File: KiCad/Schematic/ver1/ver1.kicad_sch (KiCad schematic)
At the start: 1 part

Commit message: Deez nuts
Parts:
- added U1: AD797, symbol Amplifier_Operational:AD797
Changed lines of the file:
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@@
+		)
+	)
+	(symbol
+		(lib_id "Amplifier_Operational:AD797")
+		(at 165.1 71.12 0)
+		(unit 1)
+		(exclude_from_sim no)
+		(in_bom yes)
+		(on_board yes)
+		(dnp no)
+		(fields_autoplaced yes)
+		(property "Reference" "U1"
+			(at 175.26 64.8014 0)
+			(effects
+				(font
+					(size 1.27 1.27)
+				)
+			)
+		)
+		(property "Value" "AD797"
+			(at 175.26 67.3414 0)
+			(effects
+				(font
+					(size 1.27 1.27)
+				)
+			)
+		)
+		(property "Footprint" ""
+			(at 166.37 69.85 0)
+			(effects
+				(font
+					(size 1.27 1.27)
+				)
+				(hide yes)
+			)
+		)
+		(property "Datasheet" "https://www.analog.com/media/en/technical-documentation/data-sheets/AD797.pdf"
+			(at 166.37 67.31 0)
+			(effects
+				(font
+					(size 1.27 1.27)
+				)
+				(hide yes)
+			)
+		)
+		(property "Description" "Ultralow Distortion, Ultralow Noise Op Amp, DIP-8/SOIC-8"
+			(at 165.1 71.12 0)
+			(effects
+				(font
+					(size 1.27 1.27)
+				)
+				(hide yes)
+			)
+		)
+		(pin "3"
+		)
+		(pin "2"
+		)
+		(pin "5"
+		)
+		(pin "8"
+		)
+		(pin "1"
+		)
+		(pin "6"
+		)
+		(pin "4"
+		)
+		(pin "7"
+		)
+		(instances
+			(project ""
+				(path "/7dc9043a-ef1d-4623-9acc-dd1f81d56424"
+					(reference "U1")
+					(unit 1)
+				)
+			)
 		)
 	)

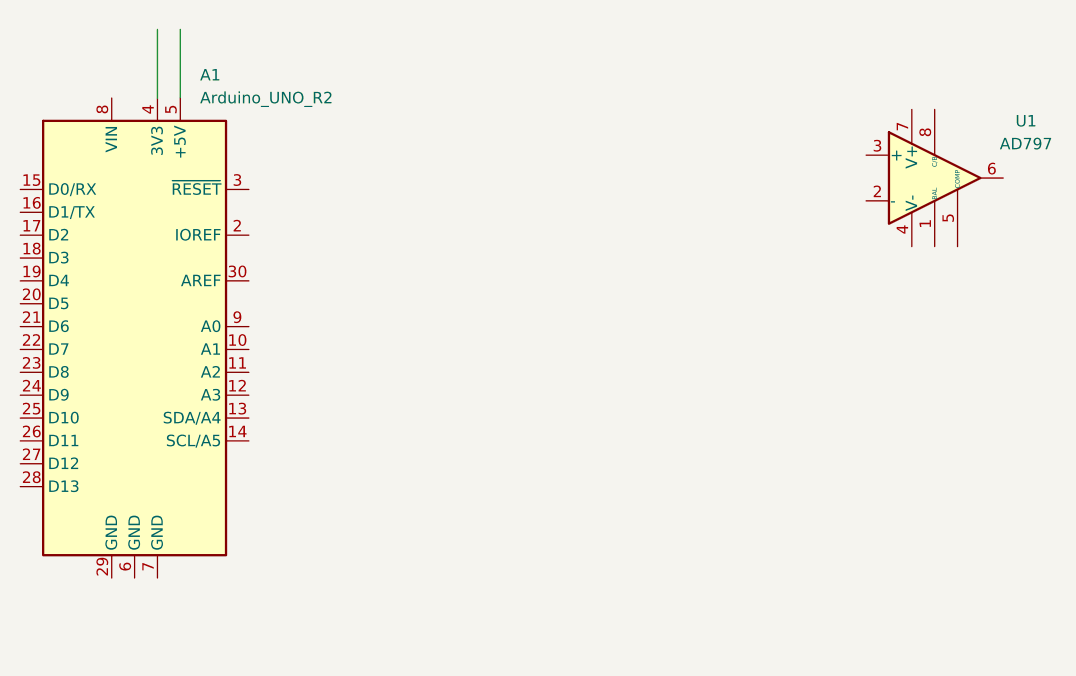
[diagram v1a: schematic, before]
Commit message: setting up arduino
battery source
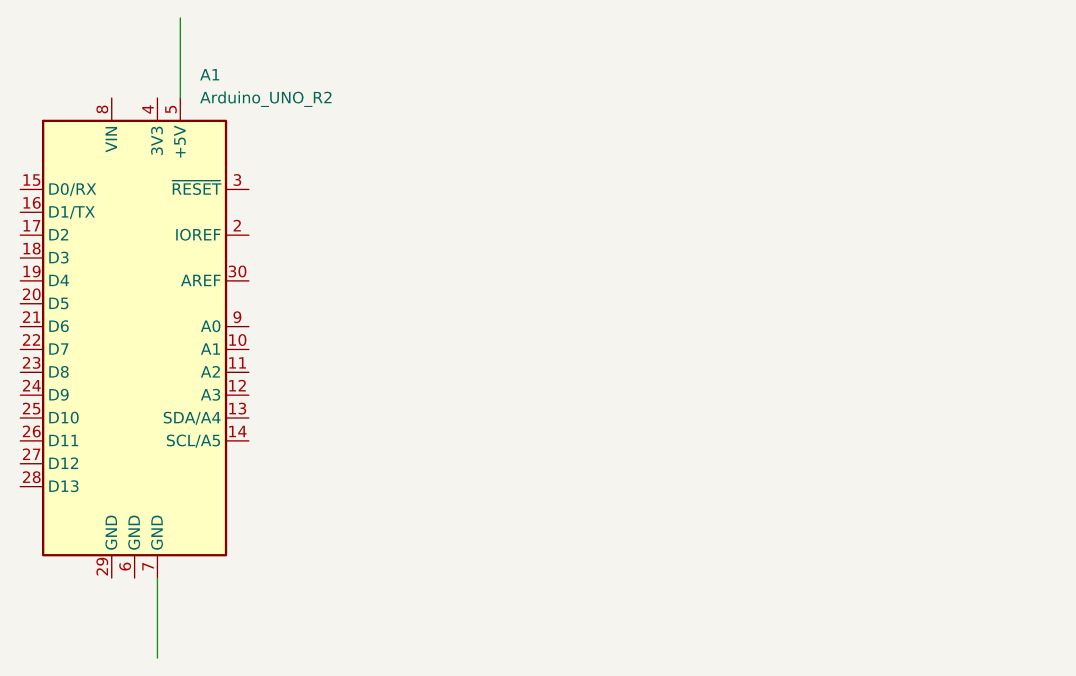
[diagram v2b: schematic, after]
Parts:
- removed U1: AD797, symbol Amplifier_Operational:AD797
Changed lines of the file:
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@@
 	(wire
 		(pts
-			(xy 78.74 54.61) (xy 78.74 62.23)
+			(xy 81.28 53.34) (xy 81.28 62.23)
 		)
 		(stroke
@@
 	(wire
 		(pts
-			(xy 81.28 54.61) (xy 81.28 62.23)
+			(xy 78.74 115.57) (xy 78.74 124.46)
 		)
 		(stroke
@@
 					(unit 1)
 				)
-			)
-		)
-	)
-	(symbol
-		(lib_id "Amplifier_Operational:AD797")
-		(at 165.1 71.12 0)
-		(unit 1)
-		(exclude_from_sim no)
-		(in_bom yes)
-		(on_board yes)
-		(dnp no)
-		(fields_autoplaced yes)
-		(property "Reference" "U1"
-			(at 175.26 64.8014 0)
-			(effects
-				(font
-					(size 1.27 1.27)
-				)
-			)
-		)
-		(property "Value" "AD797"
-			(at 175.26 67.3414 0)
-			(effects
-				(font
-					(size 1.27 1.27)
-				)
-			)
-		)
-		(property "Footprint" ""
-			(at 166.37 69.85 0)
-			(effects
-				(font
-					(size 1.27 1.27)
-				)
-				(hide yes)
-			)
-		)
-		(property "Datasheet" "https://www.analog.com/media/en/technical-documentation/data-sheets/AD797.pdf"
-			(at 166.37 67.31 0)
-			(effects
-				(font
-					(size 1.27 1.27)
-				)
-				(hide yes)
-			)
-		)
-		(property "Description" "Ultralow Distortion, Ultralow Noise Op Amp, DIP-8/SOIC-8"
-			(at 165.1 71.12 0)
-			(effects
-				(font
-					(size 1.27 1.27)
-				)
-				(hide yes)
-			)
-		)
-		(pin "3"
-		)
-		(pin "2"
-		)
-		(pin "5"
-		)
-		(pin "8"
-		)
-		(pin "1"
-		)
-		(pin "6"
-		)
-		(pin "4"
-		)
-		(pin "7"
-		)
-		(instances
-			(project ""
-				(path "/7dc9043a-ef1d-4623-9acc-dd1f81d56424"
-					(reference "U1")
-					(unit 1)
-				)

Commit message: did somethings...
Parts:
- removed A1: Arduino_UNO_R2, Module:Arduino_UNO_R2, symbol MCU_Module:Arduino_UNO_R2
- added C1: ~, symbol SparkFun Qwiic Soil Moisture Sensor-eagle-import:C-0201
- added J1: ~, SparkFun-Switch:Slide_DPDT_SMD_9.0x3.6mm, symbol SparkFun Qwiic Soil Moisture Sensor-eagle-import:JST-SH-4P-1.0
- added JP1: ~, SparkFun Qwiic Soil Moisture Sensor:2X03, symbol SparkFun Qwiic Soil Moisture Sensor-eagle-import:PINHD-2X3
- added U1: ~, SparkFun Qwiic Soil Moisture Sensor:SO08-EIAJ_MCU, symbol SparkFun Qwiic Soil Moisture Sensor-eagle-import:ATTINY85-ARDUINOTINY85-20-SMT
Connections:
- new net: J1.3 (SDA), JP1.4, U1.5 (~{(SDA/MOSI})0)
- new net: J1.4 (SCL), JP1.3, U1.7 ((SCL/SCK/A1)2)
- new net: JP1.1, U1.6 (~{(MISO})1)
- new net: JP1.5, U1.1 ((~{RESET}/A0)5)
- new net +3.3V: C1.1, J1.2 (VCC), JP1.2, U1.8 (VCC)
- new net Earth: C1.2, J1.1 (GND), J1.NC1 (5), J1.NC2 (6), JP1.6, U1.4 (GND)
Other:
- note added: "07.07.2024"
- note added: "Patrick"
- note added: "Plantifier - Ardunio Prototype"
- note added: "Samuel"
- note added: "alpha-001"

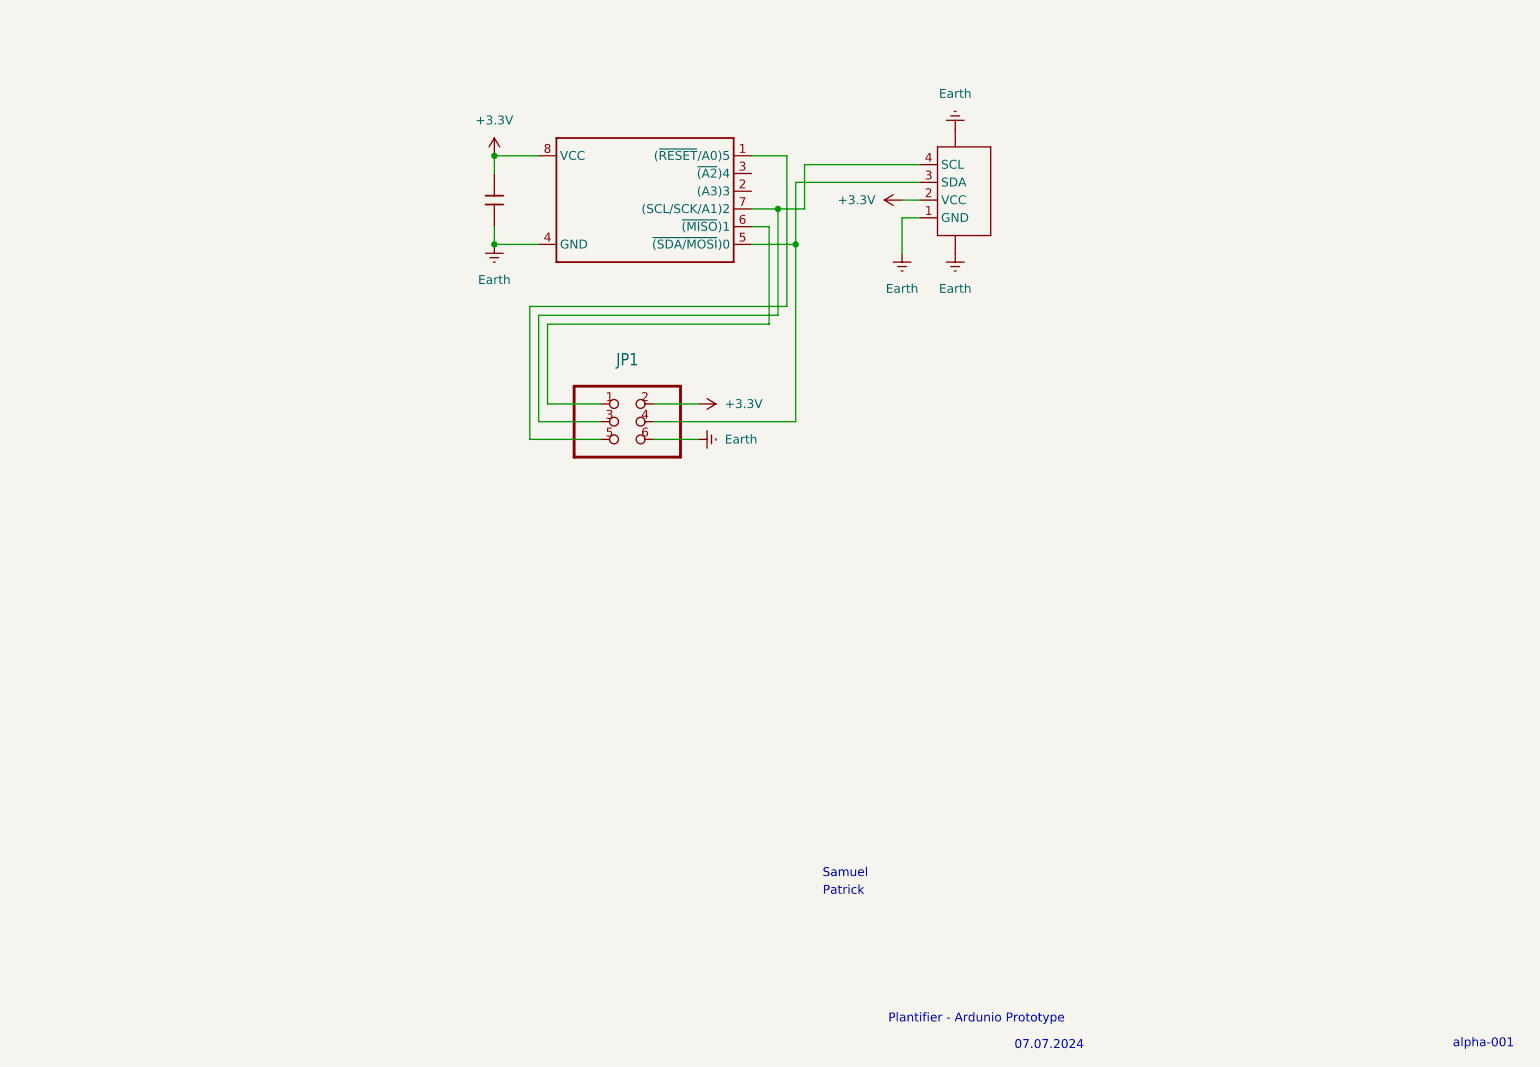
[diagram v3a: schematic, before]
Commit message: Mild Setup for Arduino on VSCode + More Schematic
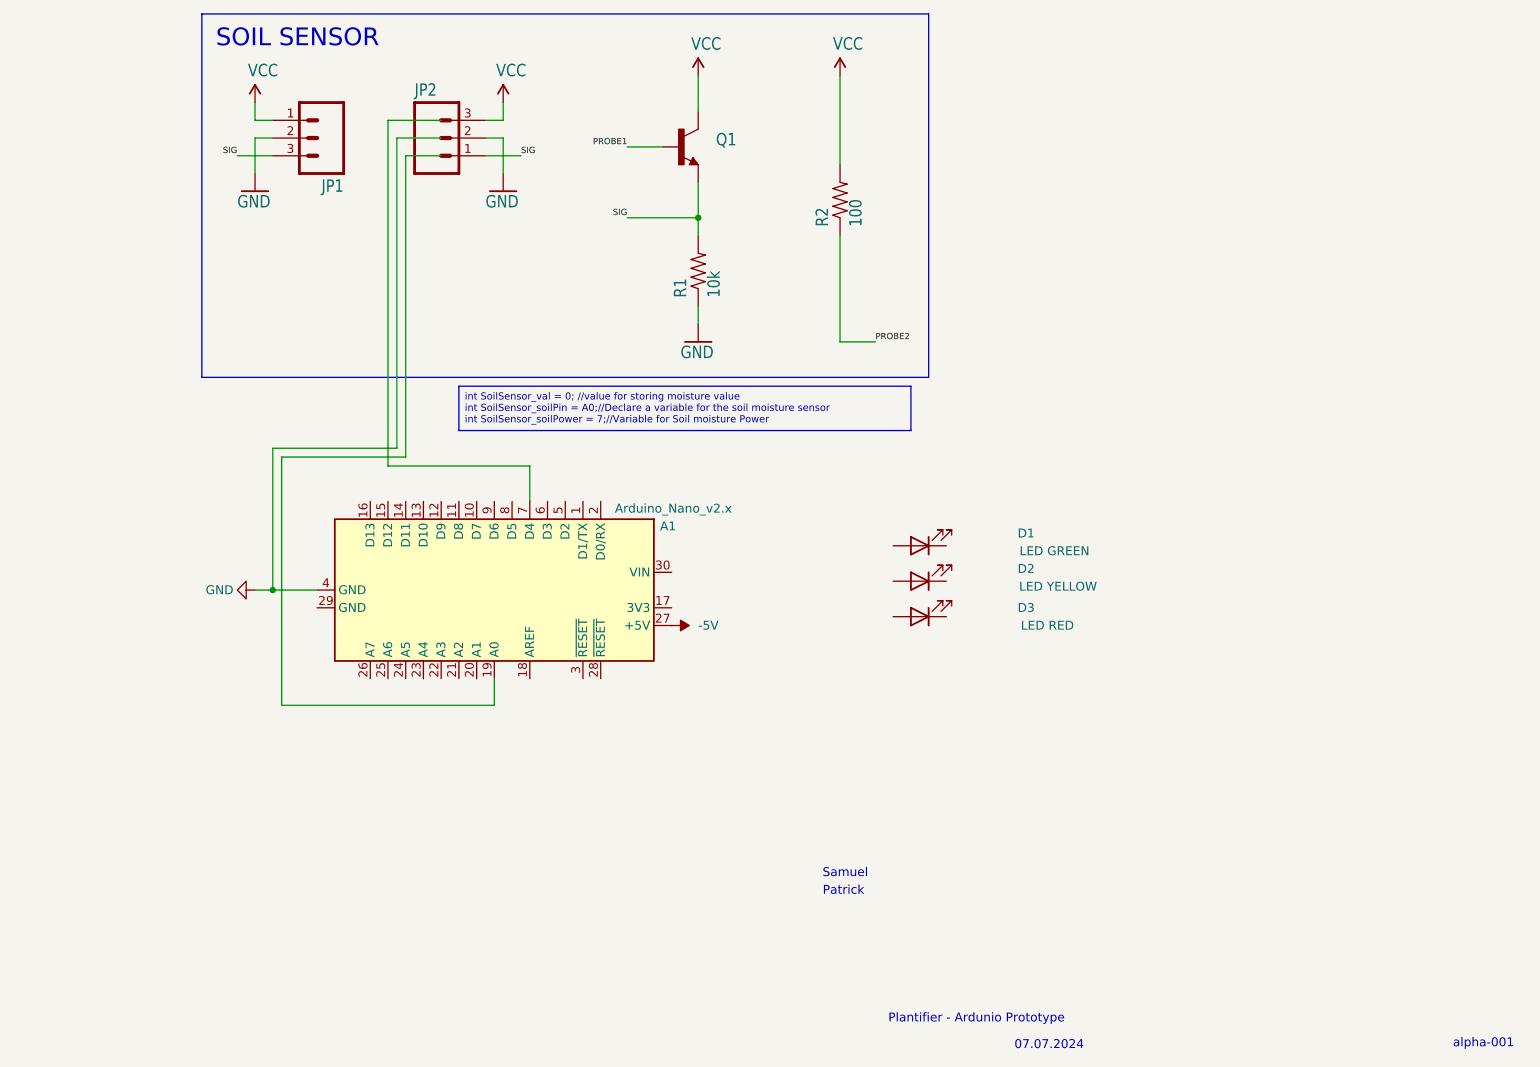
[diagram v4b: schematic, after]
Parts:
- removed C1: ~, symbol SparkFun Qwiic Soil Moisture Sensor-eagle-import:C-0201
- removed J1: ~, SparkFun-Switch:Slide_DPDT_SMD_9.0x3.6mm, symbol SparkFun Qwiic Soil Moisture Sensor-eagle-import:JST-SH-4P-1.0
- removed JP1: ~, SparkFun Qwiic Soil Moisture Sensor:2X03, symbol SparkFun Qwiic Soil Moisture Sensor-eagle-import:PINHD-2X3
- removed U1: ~, SparkFun Qwiic Soil Moisture Sensor:SO08-EIAJ_MCU, symbol SparkFun Qwiic Soil Moisture Sensor-eagle-import:ATTINY85-ARDUINOTINY85-20-SMT
- added A1: Arduino_Nano_v2.x, Module:Arduino_Nano, symbol MCU_Module:Arduino_Nano_v2.x
- added D1: LED GREEN, symbol Device:LED
- added D2: LED YELLOW, symbol Device:LED
- added D3: LED RED, symbol Device:LED
- added JP1: M03POLAR, SparkFun_Soil_Moisture_Sensor:MOLEX-1X3, symbol SparkFun_Soil_Moisture_Sensor-eagle-import:M03POLAR
- added JP2: M03SCREW_LOCK, SparkFun_Soil_Moisture_Sensor:SCREWTERMINAL-3.5MM-3_LOCK.007S, symbol SparkFun_Soil_Moisture_Sensor-eagle-import:M03SCREW_LOCK
- added Q1: TRANSISTOR_NPNMMBT2222A, SparkFun_Soil_Moisture_Sensor:SOT23-3, symbol SparkFun_Soil_Moisture_Sensor-eagle-import:TRANSISTOR_NPNMMBT2222A
- added R1: 10k, SparkFun_Soil_Moisture_Sensor:0603-RES, symbol SparkFun_Soil_Moisture_Sensor-eagle-import:100OHM-1/4W-5%(0603)
- added R2: 100, SparkFun_Soil_Moisture_Sensor:0603-RES, symbol SparkFun_Soil_Moisture_Sensor-eagle-import:100OHM-1/4W-5%(0603)
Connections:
- new net -5V: A1.27 (+5V)
- new net GND: A1.4 (GND), JP1.2, JP2.2, R1.1
- new net PROBE1: Q1.1 (B)
- new net PROBE2: R2.1
- new net SIG: JP1.3, JP2.1, Q1.2 (E), R1.2
- new net VCC: JP1.1, JP2.3, Q1.3 (C), R2.2
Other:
- note added: "SOIL SENSOR"
